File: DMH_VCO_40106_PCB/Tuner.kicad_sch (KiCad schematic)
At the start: 32 parts, among them J300 AVR-ISP-6, SW3 SW_SPDT_321_OnOff, U5 ATtiny4313-P, U6 SM420561N

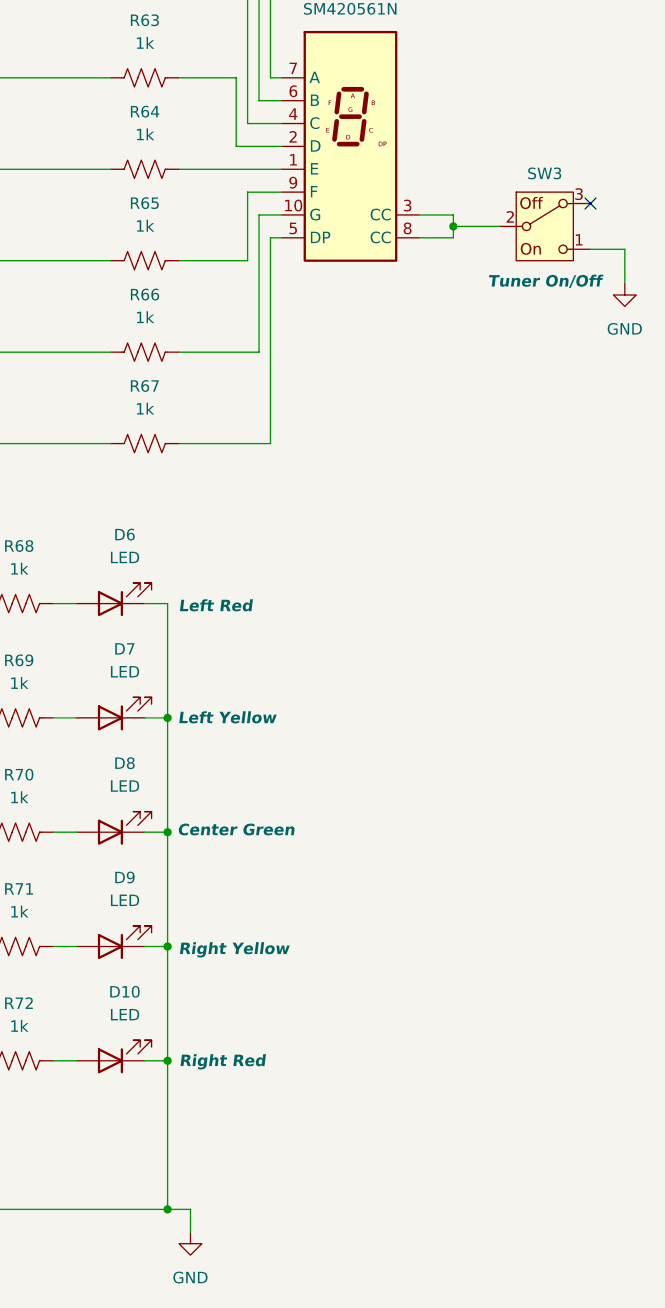
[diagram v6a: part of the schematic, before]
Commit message: Connected LEDs to Tuner On/off switch
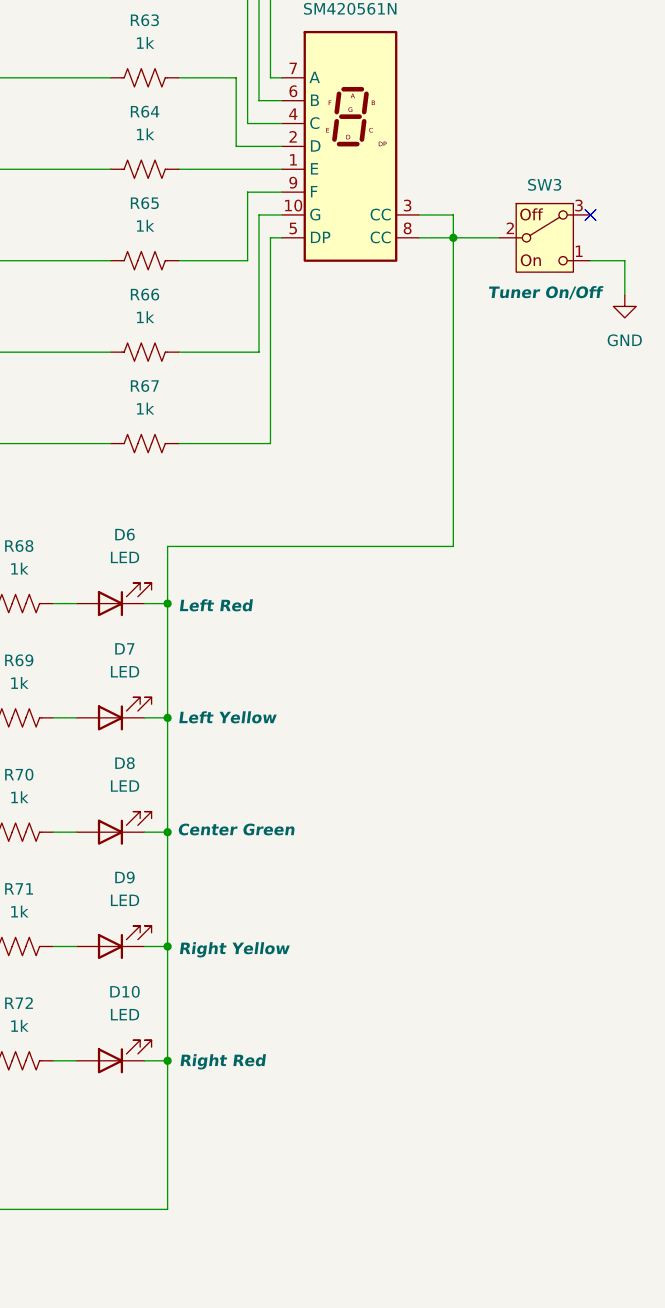
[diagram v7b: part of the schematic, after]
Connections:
- net GND: no longer D10.1 (K), D11.1 (K), D6.1 (K), D7.1 (K), D8.1 (K), D9.1 (K)
- net at SW3.2 (B), U6.3 (CC), U6.8 (CC): now also D10.1 (K), D11.1 (K), D6.1 (K), D7.1 (K), D8.1 (K), D9.1 (K)
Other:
- moved on the sheet: SW3
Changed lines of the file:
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@@
 	)
 	(junction
-		(at 86.36 128.27)
+		(at 162.56 120.65)
 		(diameter 0)
 		(color 0 0 0 0)
 	)
 	(junction
-		(at 63.5 128.27)
+		(at 86.36 128.27)
 		(diameter 0)
 		(color 0 0 0 0)
 	)
 	(junction
-		(at 162.56 187.96)
+		(at 63.5 128.27)
 		(diameter 0)
 		(color 0 0 0 0)
@@
 	)
 	(junction
-		(at 83.82 130.81)
+		(at 194.31 80.01)
 		(diameter 0)
 		(color 0 0 0 0)
 	)
 	(junction
-		(at 93.98 31.75)
+		(at 83.82 130.81)
 		(diameter 0)
 		(color 0 0 0 0)
 	)
 	(junction
-		(at 194.31 78.74)
+		(at 93.98 31.75)
 		(diameter 0)
 		(color 0 0 0 0)
@@
 	)
 	(no_connect
-		(at 209.55 76.2)
+		(at 209.55 77.47)
 	)
 	(no_connect
@@
 	(wire
 		(pts
+			(xy 194.31 114.3) (xy 194.31 80.01)
+		)
+		(stroke
+			(width 0)
+			(type default)
+		)
+	)
+	(wire
+		(pts
 			(xy 163.83 72.39) (xy 175.26 72.39)
 		)
@@
 	(wire
 		(pts
-			(xy 209.55 81.28) (xy 213.36 81.28)
+			(xy 209.55 82.55) (xy 213.36 82.55)
 		)
 		(stroke
@@
 	(wire
 		(pts
+			(xy 162.56 120.65) (xy 162.56 114.3)
+		)
+		(stroke
+			(width 0)
+			(type default)
+		)
+	)
+	(wire
+		(pts
 			(xy 173.99 62.23) (xy 175.26 62.23)
 		)
@@
 	(wire
 		(pts
-			(xy 194.31 78.74) (xy 194.31 80.01)
+			(xy 194.31 77.47) (xy 194.31 80.01)
+		)
+		(stroke
+			(width 0)
+			(type default)
+		)
+	)
+	(wire
+		(pts
+			(xy 162.56 114.3) (xy 194.31 114.3)
 		)
 		(stroke
@@
 	(wire
 		(pts
-			(xy 213.36 81.28) (xy 213.36 85.09)
+			(xy 213.36 82.55) (xy 213.36 86.36)
 		)
 		(stroke
@@
 	(wire
 		(pts
-			(xy 194.31 78.74) (xy 199.39 78.74)
+			(xy 194.31 80.01) (xy 199.39 80.01)
 		)
 		(stroke
@@
 	(wire
 		(pts
-			(xy 194.31 77.47) (xy 194.31 78.74)
-		)
-		(stroke
-			(width 0)
-			(type default)
-		)
-	)
-	(wire
-		(pts
 			(xy 45.72 152.4) (xy 81.28 152.4)
 		)
@@
 	(wire
 		(pts
-			(xy 165.1 187.96) (xy 165.1 190.5)
-		)
-		(stroke
-			(width 0)
-			(type default)
-		)
-	)
-	(wire
-		(pts
-			(xy 162.56 187.96) (xy 165.1 187.96)
-		)
-		(stroke
-			(width 0)
-			(type default)
-		)
-	)
-	(wire
-		(pts
 			(xy 142.24 146.05) (xy 134.62 146.05)
 		)
@@
 	)
 	(symbol
-		(lib_id "power:GND")
-		(at 165.1 190.5 0)
-		(unit 1)
-		(exclude_from_sim no)
-		(in_bom yes)
-		(on_board yes)
-		(dnp no)
-		(fields_autoplaced yes)
-		(property "Reference" "#PWR061"
-			(at 165.1 196.85 0)
-			(effects
-				(font
-					(size 1.27 1.27)
-				)
-				(hide yes)
-			)
-		)
-		(property "Value" "GND"
-			(at 165.1 195.58 0)
-			(effects
-				(font
-					(size 1.27 1.27)
-				)
-			)
-		)
-		(property "Footprint" ""
-			(at 165.1 190.5 0)
-			(effects
-				(font
-					(size 1.27 1.27)
-				)
-				(hide yes)
-			)
-		)
-		(property "Datasheet" ""
-			(at 165.1 190.5 0)
-			(effects
-				(font
-					(size 1.27 1.27)
-				)
-				(hide yes)
-			)
-		)
-		(property "Description" "Power symbol creates a global label with name \"GND\" , ground"
-			(at 165.1 190.5 0)
-			(effects
-				(font
-					(size 1.27 1.27)
-				)
-				(hide yes)
-			)
-		)
-		(pin "1"
-		)
-		(instances
-			(project "DMH_VCO_40106_PCB"
-				(path "/fefed352-c100-4617-bbfb-c55e7427b122/ec8b77a2-f589-4806-8224-6b0ccc79bab4"
-					(reference "#PWR061")
-					(unit 1)
-				)
-			)
-		)
-	)
-	(symbol
 		(lib_id "Device:LED")
 		(at 156.21 171.45 180)
@@
 	(symbol
 		(lib_id "SynthStuff:SW_SPDT_321_OnOff")
-		(at 204.47 78.74 0)
+		(at 204.47 80.01 0)
 		(unit 1)
 		(exclude_from_sim no)
@@
 		(dnp no)
 		(property "Reference" "SW3"
-			(at 204.47 72.898 0)
+			(at 204.47 74.168 0)
 			(effects
 				(font
@@
 		)
 		(property "Value" "SW_SPDT_321_OnOff"
-			(at 204.47 83.82 0)
+			(at 204.47 85.09 0)
 			(effects
 				(font
@@
 		)
 		(property "Footprint" "SynthStuff:Toggle_Switch_THT"
-			(at 204.47 88.9 0)
+			(at 204.47 90.17 0)
 			(effects
 				(font
@@
 		)
 		(property "Datasheet" "~"
-			(at 204.47 86.36 0)
+			(at 204.47 87.63 0)
 			(effects
 				(font
@@
 		)
 		(property "Description" "Switch, single pole double throw"
-			(at 204.47 78.74 0)
+			(at 204.47 80.01 0)
 			(effects
 				(font
@@
 		)
 		(property "Function" "Tuner On/Off"
-			(at 204.47 84.836 0)
+			(at 204.47 86.106 0)
 			(effects
 				(font
@@
 	(symbol
 		(lib_id "power:GND")
-		(at 213.36 85.09 0)
+		(at 213.36 86.36 0)
 		(unit 1)
 		(exclude_from_sim no)
@@
 		(fields_autoplaced yes)
 		(property "Reference" "#PWR058"
-			(at 213.36 91.44 0)
+			(at 213.36 92.71 0)
 			(effects
 				(font
@@
 		)
 		(property "Value" "GND"
-			(at 213.36 90.17 0)
+			(at 213.36 91.44 0)
 			(effects
 				(font
@@
 		)
 		(property "Footprint" ""
-			(at 213.36 85.09 0)
+			(at 213.36 86.36 0)
 			(effects
 				(font
@@
 		)
 		(property "Datasheet" ""
-			(at 213.36 85.09 0)
+			(at 213.36 86.36 0)
 			(effects
 				(font
@@
 		)
 		(property "Description" "Power symbol creates a global label with name \"GND\" , ground"
-			(at 213.36 85.09 0)
+			(at 213.36 86.36 0)
 			(effects
 				(font

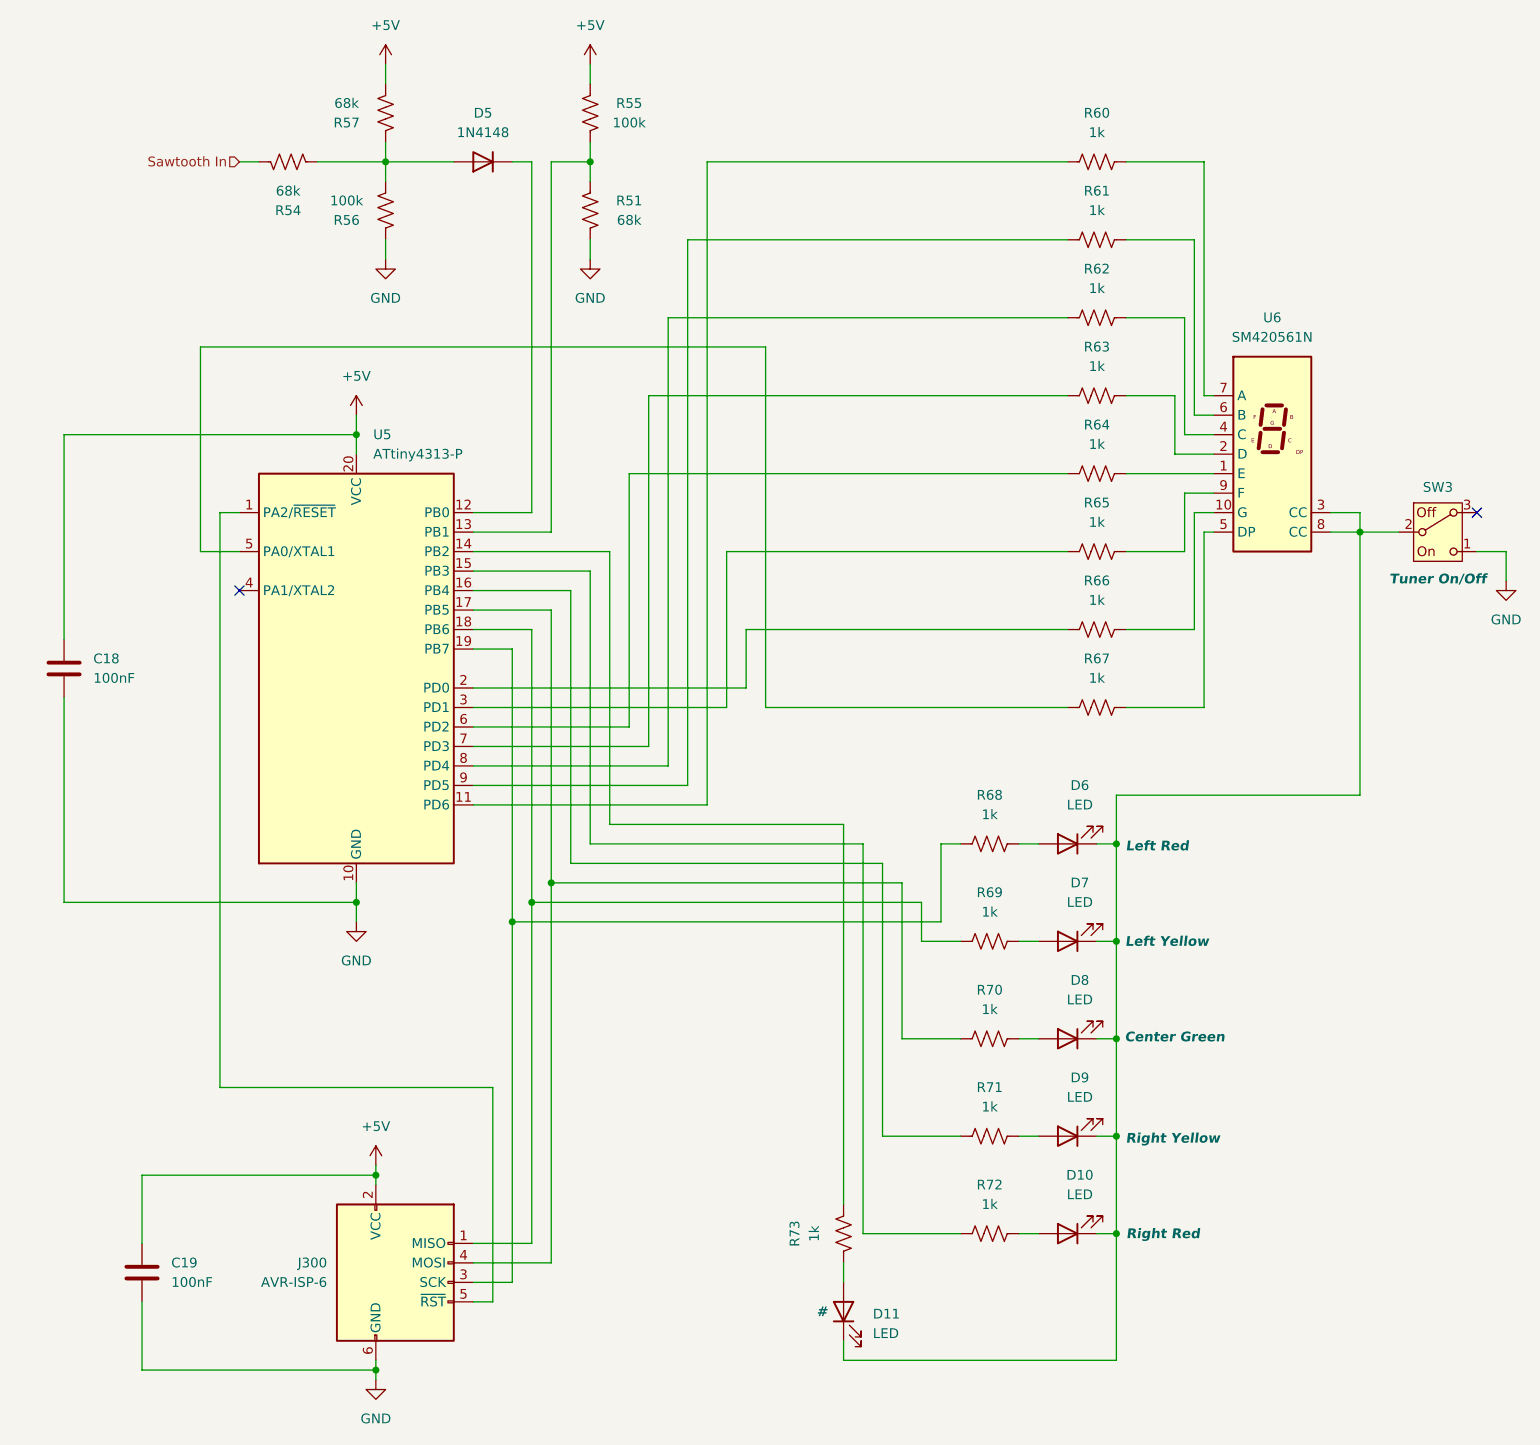
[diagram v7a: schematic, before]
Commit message: Connected tuner switch to uC GPIO pin
... and all LED and display segments directly to GND
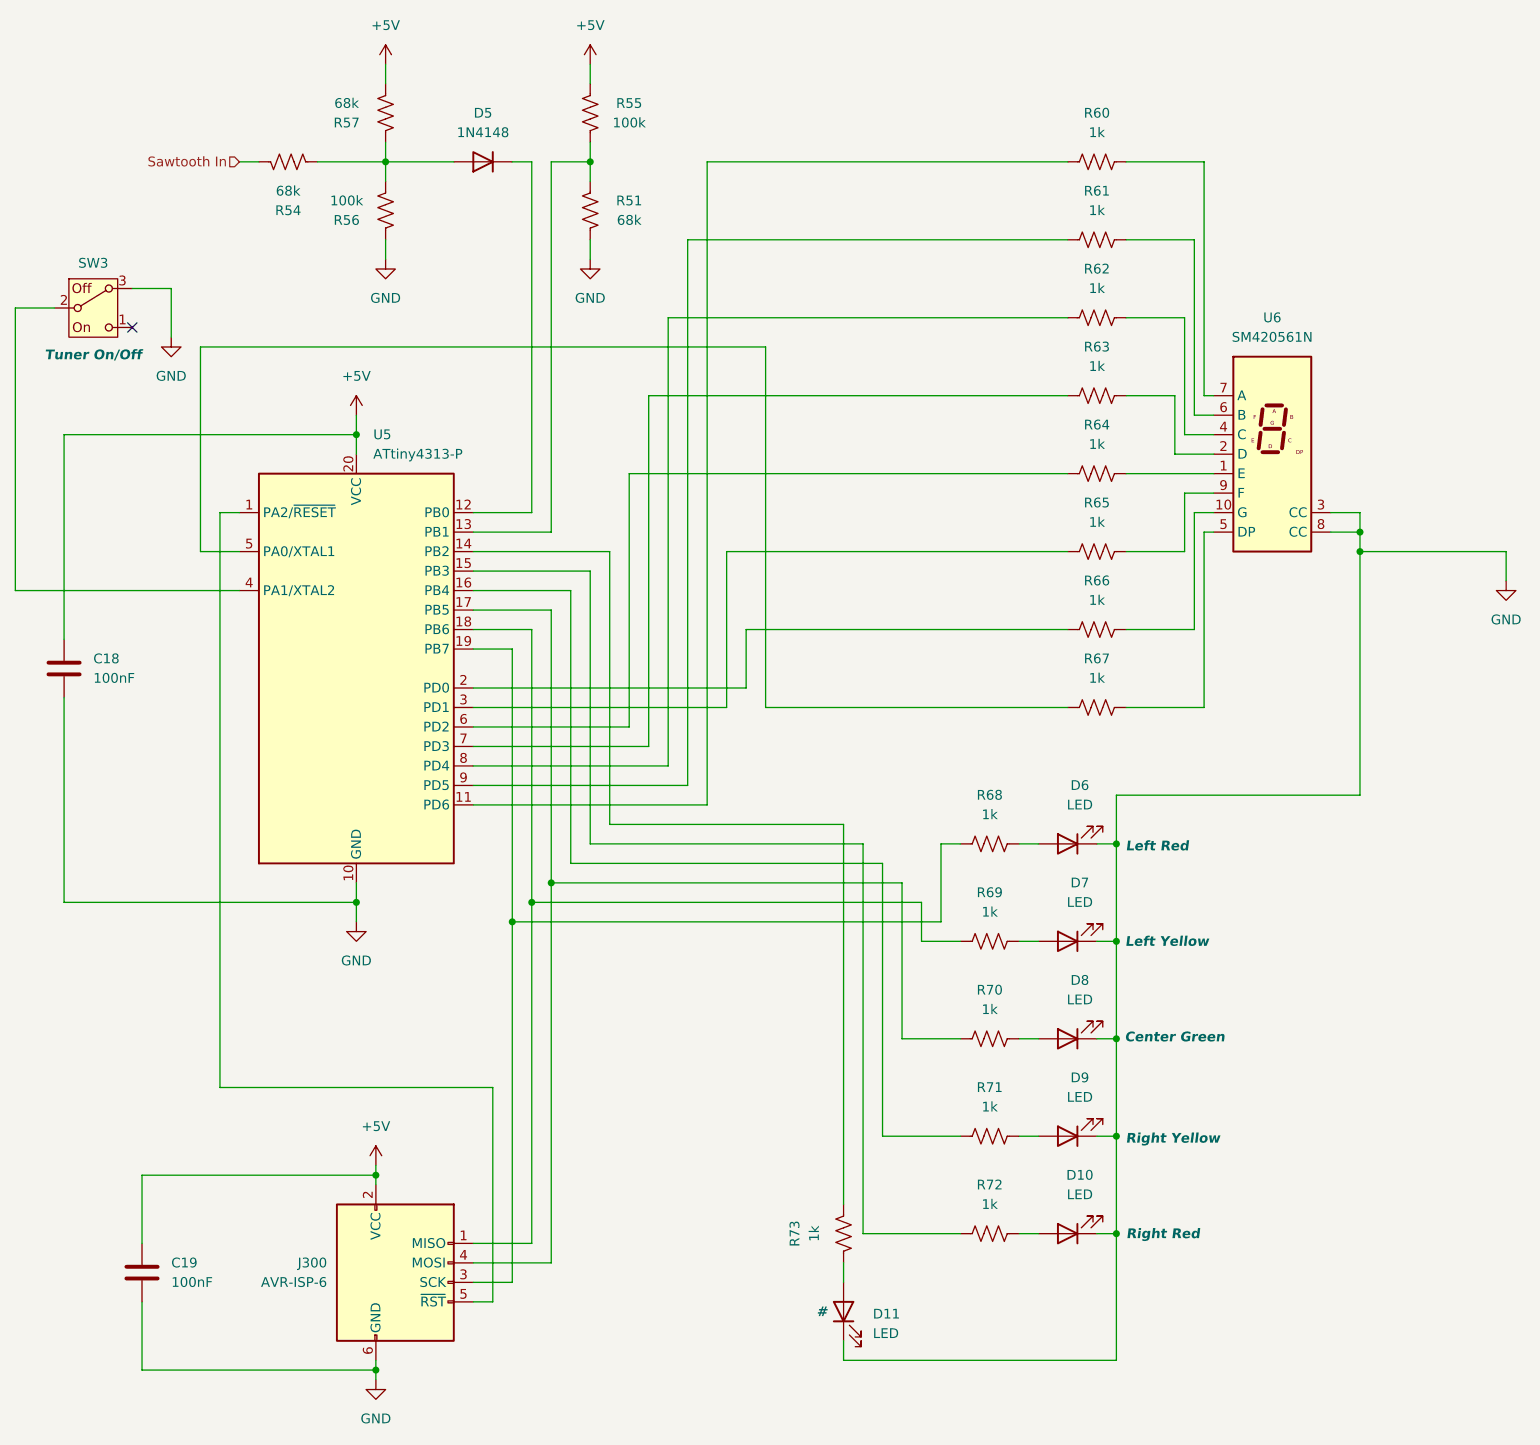
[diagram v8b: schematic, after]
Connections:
- net GND: now also D10.1 (K), D11.1 (K), D6.1 (K), D7.1 (K), D8.1 (K), D9.1 (K), SW3.3 (A), U6.3 (CC), U6.8 (CC); no longer SW3.1 (C)
- net at U5.4 (PA1/XTAL2): now also SW3.2 (B)
- no-connect marks 2 -> 1
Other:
- moved on the sheet: SW3
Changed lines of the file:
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@@
 	)
 	(junction
+		(at 194.31 82.55)
+		(diameter 0)
+		(color 0 0 0 0)
+	)
+	(junction
 		(at 162.56 133.35)
 		(diameter 0)
@@
 	)
 	(no_connect
-		(at 209.55 77.47)
-	)
-	(no_connect
-		(at 48.26 87.63)
+		(at 34.29 53.34)
 	)
 	(wire
 		(pts
-			(xy 194.31 114.3) (xy 194.31 80.01)
+			(xy 194.31 114.3) (xy 194.31 82.55)
 		)
 		(stroke
@@
 	(wire
 		(pts
-			(xy 209.55 82.55) (xy 213.36 82.55)
-		)
-		(stroke
-			(width 0)
-			(type default)
-		)
-	)
-	(wire
-		(pts
 			(xy 63.5 128.27) (xy 63.5 130.81)
 		)
@@
 	(wire
 		(pts
+			(xy 39.37 48.26) (xy 34.29 48.26)
+		)
+		(stroke
+			(width 0)
+			(type default)
+		)
+	)
+	(wire
+		(pts
 			(xy 170.18 62.23) (xy 170.18 69.85)
 		)
@@
 	(wire
 		(pts
+			(xy 39.37 54.61) (xy 39.37 48.26)
+		)
+		(stroke
+			(width 0)
+			(type default)
+		)
+	)
+	(wire
+		(pts
 			(xy 88.9 31.75) (xy 88.9 80.01)
 		)
@@
 	(wire
 		(pts
+			(xy 194.31 82.55) (xy 194.31 80.01)
+		)
+		(stroke
+			(width 0)
+			(type default)
+		)
+	)
+	(wire
+		(pts
 			(xy 162.56 120.65) (xy 162.56 133.35)
 		)
@@
 	(wire
 		(pts
+			(xy 194.31 82.55) (xy 213.36 82.55)
+		)
+		(stroke
+			(width 0)
+			(type default)
+		)
+	)
+	(wire
+		(pts
 			(xy 63.5 64.77) (xy 63.5 67.31)
 		)
@@
 	(wire
 		(pts
+			(xy 19.05 87.63) (xy 48.26 87.63)
+		)
+		(stroke
+			(width 0)
+			(type default)
+		)
+	)
+	(wire
+		(pts
 			(xy 213.36 82.55) (xy 213.36 86.36)
 		)
@@
 	(wire
 		(pts
+			(xy 24.13 50.8) (xy 19.05 50.8)
+		)
+		(stroke
+			(width 0)
+			(type default)
+		)
+	)
+	(wire
+		(pts
 			(xy 127 185.42) (xy 127 187.96)
 		)
@@
 	(wire
 		(pts
-			(xy 142.24 120.65) (xy 139.7 120.65)
+			(xy 19.05 50.8) (xy 19.05 87.63)
 		)
 		(stroke
@@
 	(wire
 		(pts
-			(xy 88.9 125.73) (xy 88.9 175.26)
+			(xy 142.24 120.65) (xy 139.7 120.65)
 		)
 		(stroke
@@
 	(wire
 		(pts
-			(xy 93.98 29.21) (xy 93.98 31.75)
+			(xy 88.9 125.73) (xy 88.9 175.26)
 		)
 		(stroke
@@
 	(wire
 		(pts
-			(xy 137.16 128.27) (xy 86.36 128.27)
+			(xy 93.98 29.21) (xy 93.98 31.75)
 		)
 		(stroke
@@
 	(wire
 		(pts
-			(xy 88.9 125.73) (xy 88.9 90.17)
+			(xy 137.16 128.27) (xy 86.36 128.27)
 		)
 		(stroke
@@
 	(wire
 		(pts
-			(xy 93.98 85.09) (xy 78.74 85.09)
+			(xy 88.9 125.73) (xy 88.9 90.17)
 		)
 		(stroke
@@
 	(wire
 		(pts
-			(xy 194.31 80.01) (xy 199.39 80.01)
+			(xy 93.98 85.09) (xy 78.74 85.09)
 		)
 		(stroke
@@
 	(symbol
 		(lib_id "SynthStuff:SW_SPDT_321_OnOff")
-		(at 204.47 80.01 0)
+		(at 29.21 50.8 0)
 		(unit 1)
 		(exclude_from_sim no)
@@
 		(dnp no)
 		(property "Reference" "SW3"
-			(at 204.47 74.168 0)
+			(at 29.21 44.958 0)
 			(effects
 				(font
@@
 		)
 		(property "Value" "SW_SPDT_321_OnOff"
-			(at 204.47 85.09 0)
+			(at 29.21 55.88 0)
 			(effects
 				(font
@@
 		)
 		(property "Footprint" "SynthStuff:Toggle_Switch_THT"
-			(at 204.47 90.17 0)
+			(at 29.21 60.96 0)
 			(effects
 				(font
@@
 		)
 		(property "Datasheet" "~"
-			(at 204.47 87.63 0)
+			(at 29.21 58.42 0)
 			(effects
 				(font
@@
 		)
 		(property "Description" "Switch, single pole double throw"
-			(at 204.47 80.01 0)
+			(at 29.21 50.8 0)
 			(effects
 				(font
@@
 		)
 		(property "Function" "Tuner On/Off"
-			(at 204.47 86.106 0)
+			(at 29.21 56.896 0)
 			(effects
 				(font
@@
 					(unit 1)
 				)
+			)
+		)
+	)
+	(symbol
+		(lib_id "power:GND")
+		(at 39.37 54.61 0)
+		(unit 1)
+		(exclude_from_sim no)
+		(in_bom yes)
+		(on_board yes)
+		(dnp no)
+		(fields_autoplaced yes)
+		(property "Reference" "#PWR011"
+			(at 39.37 60.96 0)
+			(effects
+				(font
+					(size 1.27 1.27)
+				)
+				(hide yes)
+			)
+		)
+		(property "Value" "GND"
+			(at 39.37 59.69 0)
+			(effects
+				(font
+					(size 1.27 1.27)
+				)
+			)
+		)
+		(property "Footprint" ""
+			(at 39.37 54.61 0)
+			(effects
+				(font
+					(size 1.27 1.27)
+				)
+				(hide yes)
+			)
+		)
+		(property "Datasheet" ""
+			(at 39.37 54.61 0)
+			(effects
+				(font
+					(size 1.27 1.27)
+				)
+				(hide yes)
+			)
+		)
+		(property "Description" "Power symbol creates a global label with name \"GND\" , ground"
+			(at 39.37 54.61 0)
+			(effects
+				(font
+					(size 1.27 1.27)
+				)
+				(hide yes)
+			)
+		)
+		(pin "1"
+		)
+		(instances
+			(project ""
+				(path "/fefed352-c100-4617-bbfb-c55e7427b122/ec8b77a2-f589-4806-8224-6b0ccc79bab4"
+					(reference "#PWR011")
+					(unit 1)
+				)
